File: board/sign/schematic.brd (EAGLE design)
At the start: 97.8 x 65.8 mm, 40 parts, among them IC1 STM32F207ZGT, IC3 LM3940, J1 DCJ0202, J3 DM3AT-SF-PEJM5, X2 22-23-2041

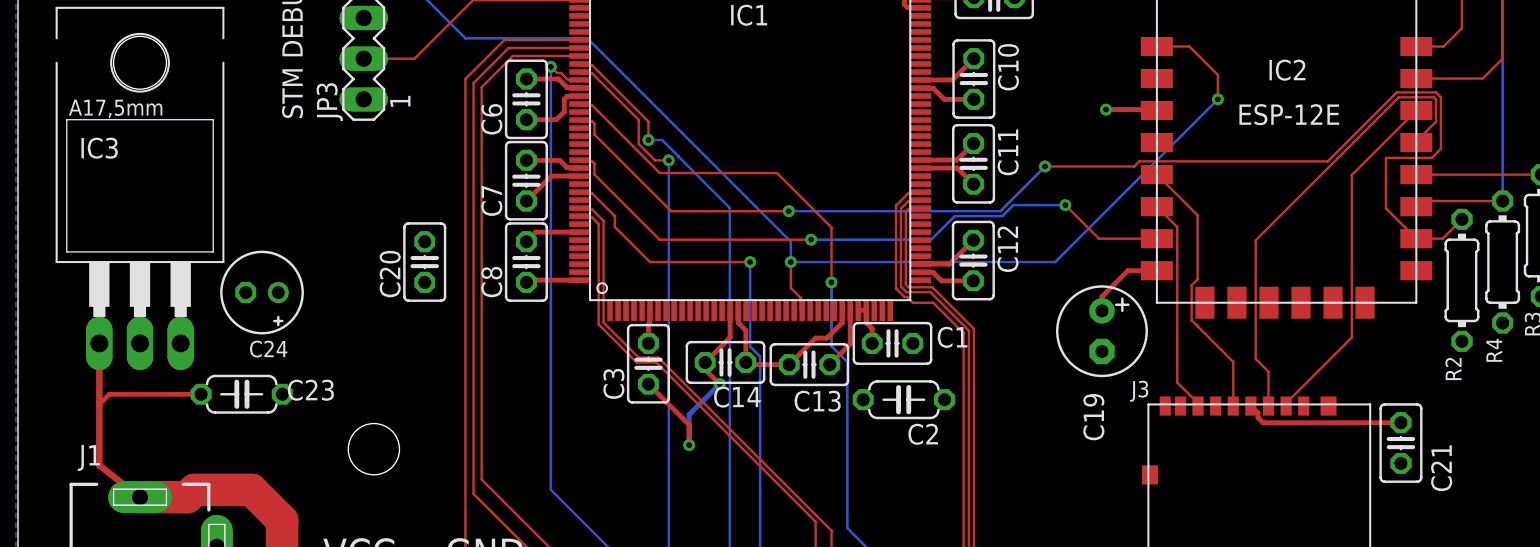
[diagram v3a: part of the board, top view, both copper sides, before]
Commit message: fix board trace widths
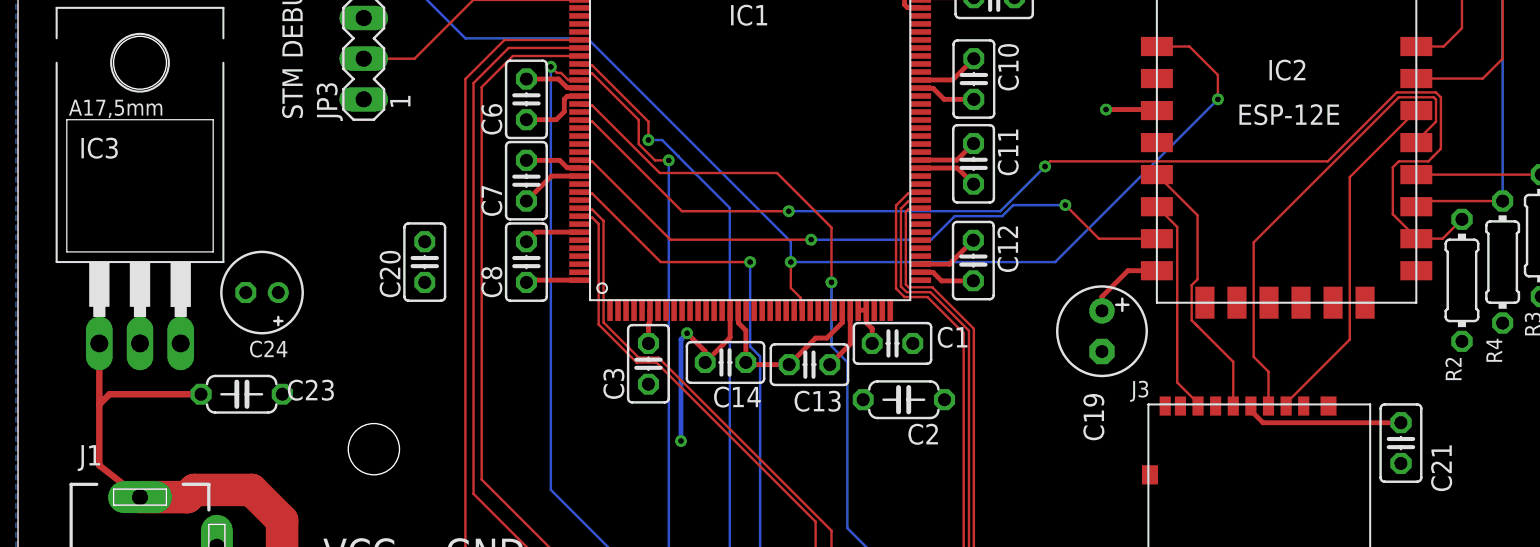
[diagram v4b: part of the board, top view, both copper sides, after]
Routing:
- net GND: track 52.5 -> 50.5 mm
- net RX: track 75.8 -> 74.5 mm

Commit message: Fix board FINAL
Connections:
- removed net N$4: C18.2, JP1.13
- net DCLK: now also C18.2, JP1.13; no longer C18.1
- net GND: now also C18.1
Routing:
- net N$4: track 7.05 -> 0.00 mm
- net DCLK: track 51.0 -> 54.6 mm
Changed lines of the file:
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@@
 <drawing>
 <settings>
-<setting alwaysvectorfont="yes"/>
+<setting alwaysvectorfont="no"/>
 <setting verticaltext="up"/>
 </settings>
@@
 <wire x1="35.1914" y1="38.9836" x2="35.8646875" y2="38.9836" width="0.1524" layer="1"/>
 <wire x1="35.8646875" y1="38.9836" x2="40.0784875" y2="34.7698" width="0.1524" layer="1"/>
-<contactref element="C18" pad="1"/>
 <wire x1="51.7906" y1="22.9657875" x2="51.7906" y2="12.5984" width="0.1524" layer="16"/>
-<wire x1="61.849" y1="5.715" x2="58.674" y2="5.715" width="0.1524" layer="16"/>
-<wire x1="58.674" y1="5.715" x2="51.7906" y2="12.5984" width="0.1524" layer="16"/>
+<wire x1="51.7906" y1="12.5984" x2="56.769" y2="7.62" width="0.1524" layer="16"/>
 <wire x1="47.3992" y1="34.7698" x2="50.8" y2="31.369" width="0.1524" layer="1"/>
 <wire x1="50.8" y1="31.369" x2="50.8" y2="27.94" width="0.1524" layer="1"/>
 <wire x1="40.0784875" y1="34.7698" x2="47.3992" y2="34.7698" width="0.1524" layer="1"/>
+<contactref element="JP1" pad="13"/>
+<contactref element="C18" pad="2"/>
+<wire x1="56.769" y1="7.62" x2="56.769" y2="5.715" width="0.1524" layer="16"/>
+<wire x1="56.769" y1="5.715" x2="54.737" y2="3.683" width="0.1524" layer="16"/>
+<wire x1="54.737" y1="3.683" x2="51.816" y2="3.683" width="0.1524" layer="16"/>
+<wire x1="51.816" y1="3.683" x2="50.8" y2="4.699" width="0.1524" layer="16"/>
+<wire x1="50.8" y1="4.699" x2="50.8" y2="5.08" width="0.1524" layer="16"/>
 </signal>
 <signal name="A">
@@
 <contactref element="J3" pad="6"/>
 <contactref element="J3" pad="MOUNT2"/>
+<contactref element="C18" pad="1"/>
 </signal>
 <signal name="+3V3">
@@
 <wire x1="37.97" y1="49.480915625" x2="39.000071875" y2="50.5109875" width="0.3048" layer="1"/>
 </signal>
-<signal name="N$4">
-<contactref element="JP1" pad="13"/>
-<contactref element="C18" pad="2"/>
-<wire x1="51.939075" y1="5.08" x2="50.8" y2="5.08" width="0.1524" layer="16"/>
-<wire x1="52.929675" y1="4.0894" x2="51.939075" y2="5.08" width="0.1524" layer="16"/>
-<wire x1="55.1434" y1="4.0894" x2="52.929675" y2="4.0894" width="0.1524" layer="16"/>
-<wire x1="56.769" y1="5.715" x2="55.1434" y2="4.0894" width="0.1524" layer="16"/>
-</signal>
 </signals>

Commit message: Actually the final board I promise
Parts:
- removed X2: 22-23-2041, con-molex:22-23-2041
- added C25: 100nF, rcl:C025-025X050
- added J2: (no value), SparkFun-Connectors:SCREWTERMINAL-5MM-2
- moved C19 4.16 mm to (63.6, 25.8)
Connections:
- net +3V3: now also C25.1
- net +5V: now also J2.1; no longer X2.1, X2.2
- net GND: now also C25.2, J2.2; no longer X2.3, X2.4
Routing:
- net +3V3: track 73.9 -> 77.1 mm
- net +5V: track 39.3 -> 38.4 mm
- net R0: track 47.6 -> 46.8 mm
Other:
- board text added: "+5V"
- board text removed: "VCC"
